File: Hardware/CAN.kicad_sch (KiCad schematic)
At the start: 20 parts, among them U1 ISOW1044

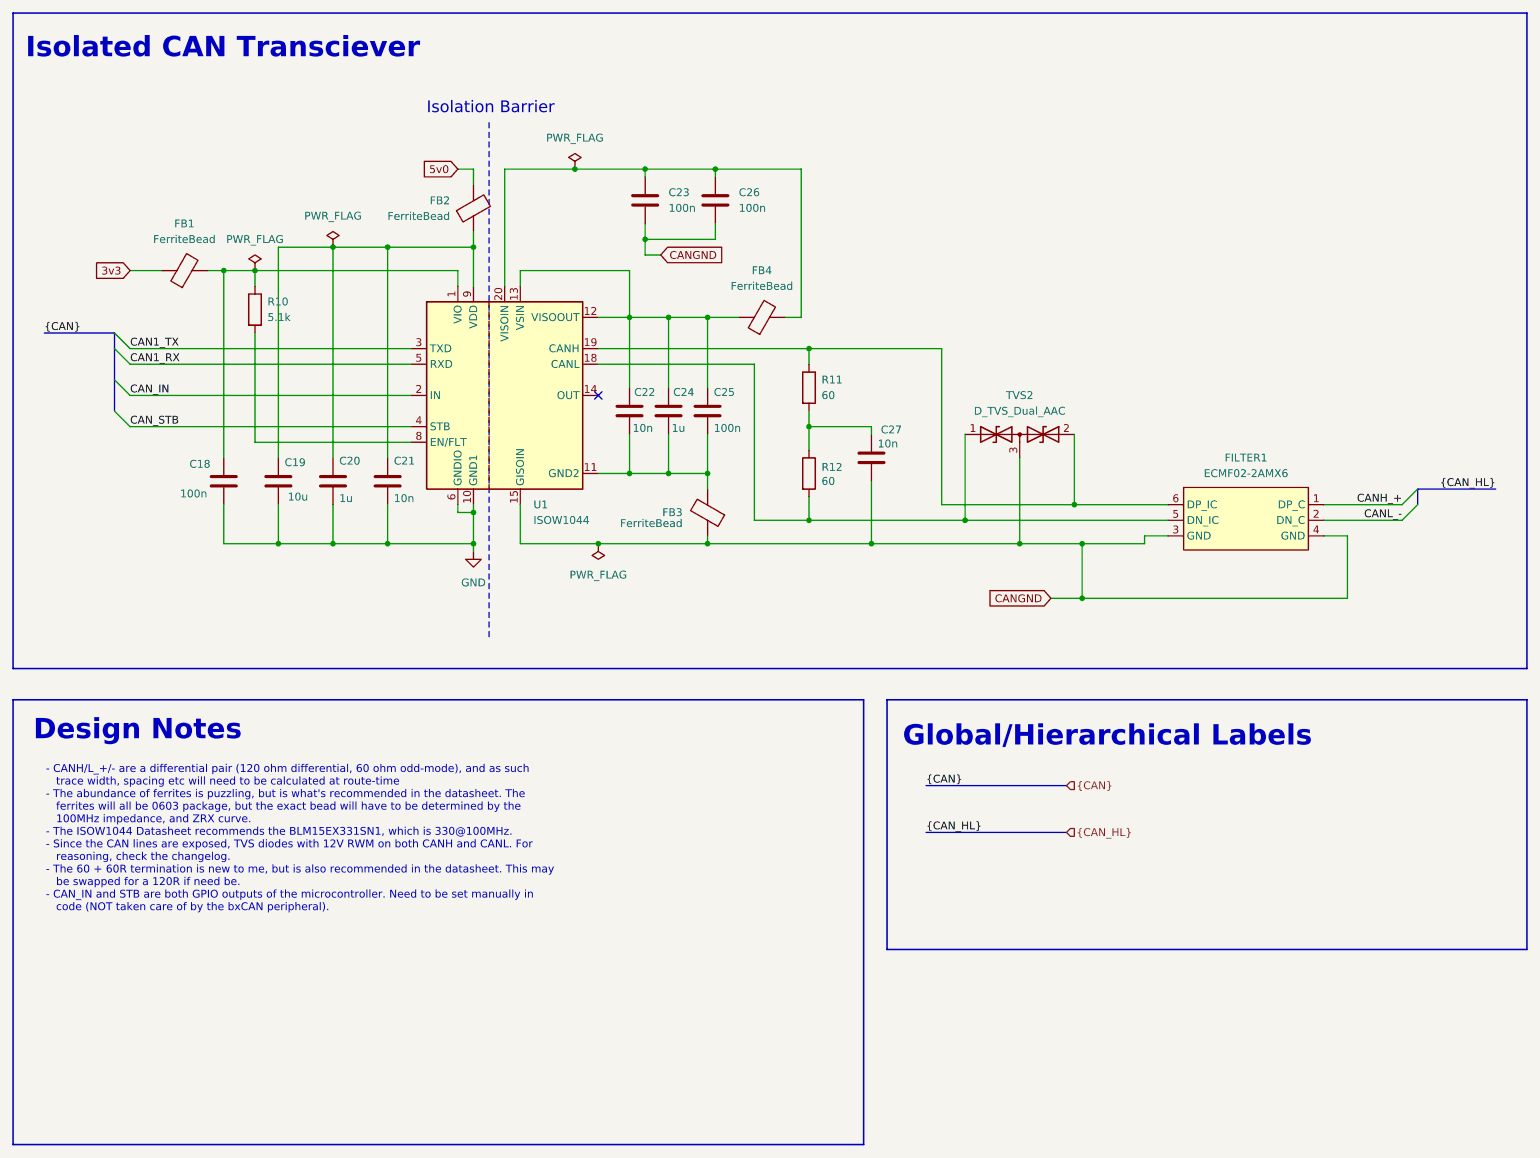
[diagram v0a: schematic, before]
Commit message: Replaced the ISOW1044 CAN Transceiver with the ISO1042 + isolated DC-DC and LDO
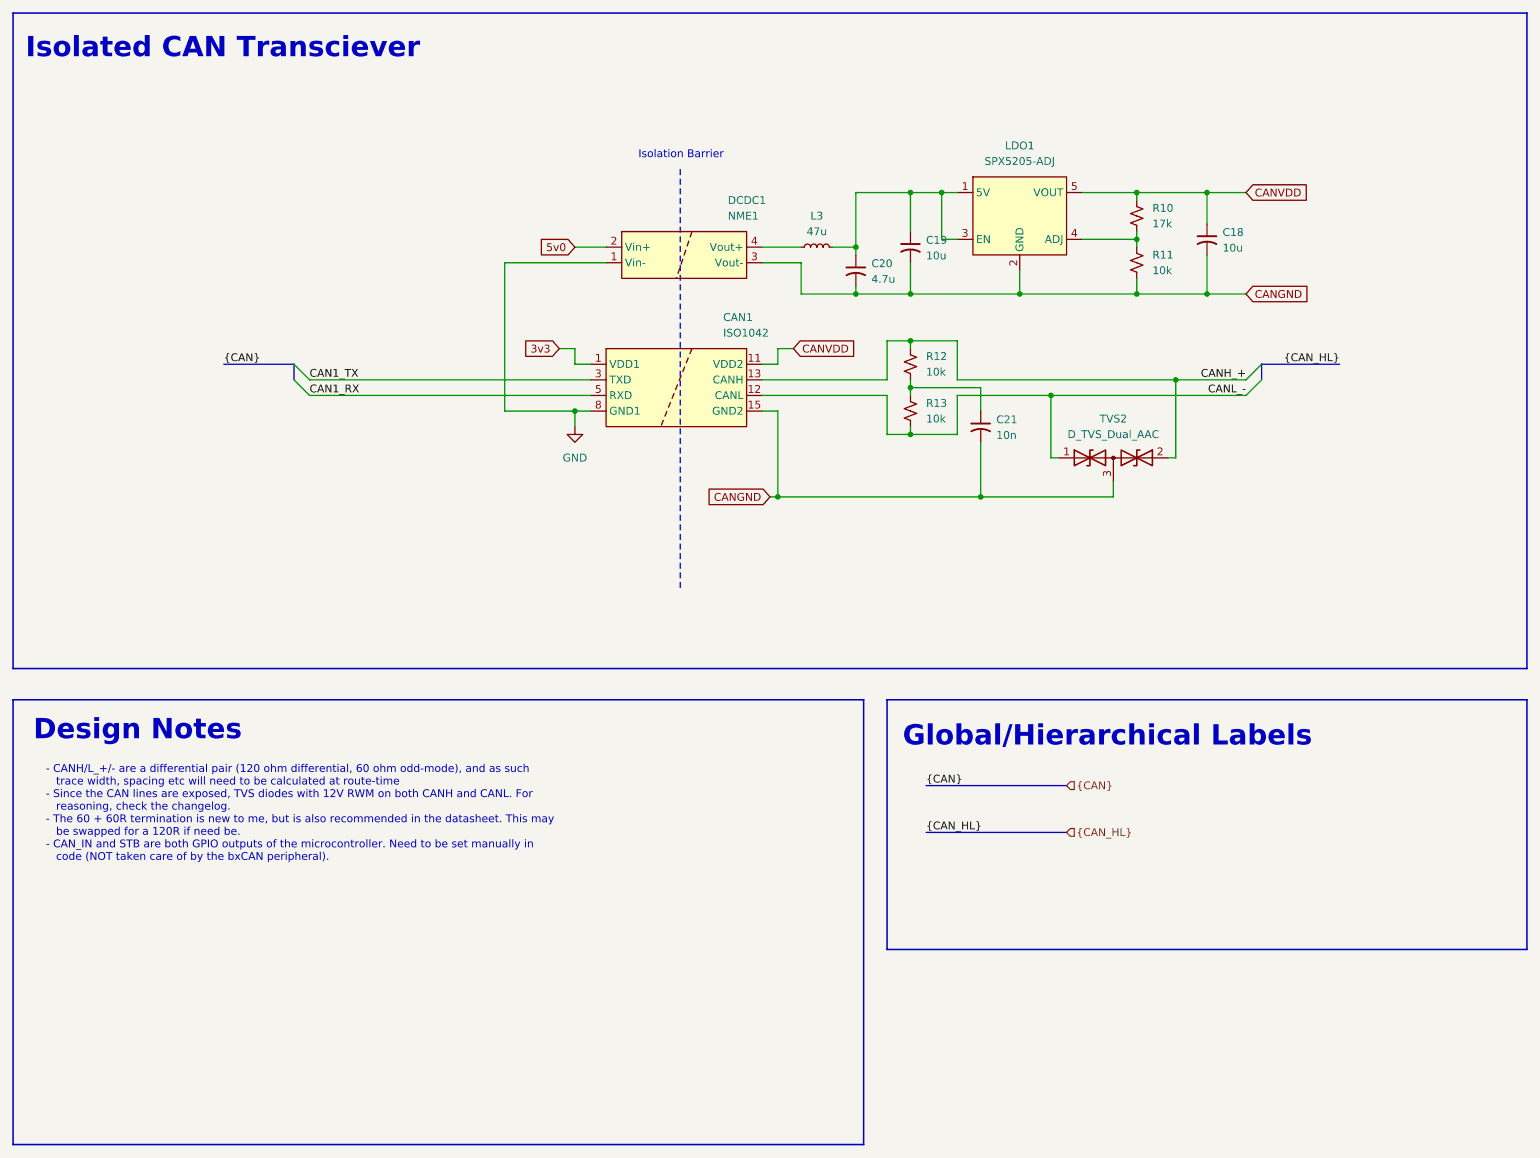
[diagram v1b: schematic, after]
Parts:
- removed C18, C23, C25, C26: 100n, Capacitor_SMD:C_0603_1608Metric_Pad1.08x0.95mm_HandSolder, symbol Device:C
- removed C19: 10u, Capacitor_SMD:C_0603_1608Metric_Pad1.08x0.95mm_HandSolder, symbol Device:C
- removed C20, C24: 1u, Capacitor_SMD:C_0603_1608Metric_Pad1.08x0.95mm_HandSolder, symbol Device:C
- removed C21, C22, C27: 10n, Capacitor_SMD:C_0603_1608Metric_Pad1.08x0.95mm_HandSolder, symbol Device:C
- removed FB1, FB2, FB3, FB4: FerriteBead, Inductor_SMD:L_0603_1608Metric_Pad1.05x0.95mm_HandSolder, symbol Device:FerriteBead
- removed FILTER1: ECMF02-2AMX6, symbol symbols:ECMF2-40A100N6
- removed R10: 5.1k, Resistor_SMD:R_0603_1608Metric_Pad0.98x0.95mm_HandSolder, symbol Device:R
- removed R11, R12: 60, Resistor_SMD:R_0603_1608Metric_Pad0.98x0.95mm_HandSolder, symbol Device:R
- removed U1: ISOW1044, Package_SO:SOIC-20W_7.5x12.8mm_P1.27mm, symbol Interface_CAN_LIN:ISOW1044
- added C18, C19: 10u, symbol Device:C_Small_US
- added C20: 4.7u, symbol Device:C_Small_US
- added C21: 10n, symbol Device:C_Small_US
- added CAN1: ISO1042, symbol symbols:ISO1042
- added DCDC1: NME1, symbol symbols:NME1
- added L3: 47u, symbol Device:L_Small
- added LDO1: SPX5205-ADJ, symbol symbols:SPX5205-ADJ
- added R10: 17k, symbol Device:R_Small_US
- added R11, R12, R13: 10k, symbol Device:R_Small_US
- TVS2: footprint Package_TO_SOT_SMD:SOT-23-3 -> (none)
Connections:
- net 3v3: now also CAN1.1 (VDD1)
- net 5v0: now also DCDC1.2 (Vin+)
- net CAN1_RX: now also CAN1.5 (RXD)
- net CAN1_TX: now also CAN1.3 (TXD)
- net CANH_+: now also TVS2.2 (A2), CAN1.13 (CANH), R12.1
- net CANL_-: now also TVS2.1 (A1), CAN1.12 (CANL), R13.2
- net GND: now also CAN1.2 (GND1), CAN1.8 (GND1), DCDC1.1 (Vin-)
- net CANGND renamed GND2
- net GND2: now also C18.2, C19.2, C20.2, C21.2, CAN1.10 (GND2), CAN1.15 (GND2), CAN1.9 (GND2), DCDC1.3 (Vout-), LDO1.2 (GND), R11.2
- new net: C21.1, R12.2, R13.1
- new net: DCDC1.4 (Vout+), L3.1
- new net: LDO1.4 (ADJ), R10.2, R11.1
- new net: C19.1, C20.1, L3.2, LDO1.1 (5V), LDO1.3 (EN)
- new net: CAN1.4, CAN1.6, CAN1.7
- new net VDD2: C18.1, CAN1.11 (VDD2), CAN1.16 (VDD2), LDO1.5 (VOUT), R10.1
- no-connect marks 1 -> 0
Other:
- note added: "- CANH/L_+/- are a differential pair (120 ohm differential, 60 ohm odd-mode), and as such trace width, spacing etc will need to be calculated at route-time - Since the CAN lines are exposed, TVS diodes with 12V RWM on both CANH and CANL. For reasoning, check the changelog. - The 60 + 60R termination is new to me, but is also recommended in the datasheet. This may be swapped for a 120R if need be.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"
- note removed: "- CANH/L_+/- are a differential pair (120 ohm differential, 60 ohm odd-mode), and as such trace width, spacing etc will need to be calculated at route-time - The abundance of ferrites is puzzling, but is what's recommended in the datasheet. The ferrites will all be 0603 package, but the exact bead will have to be determined by the 100MHz impedance, and ZRX curve. - The ISOW1044 Datasheet recommen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"

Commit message: Updated the USB-C connector from 14 pin to 16 pin
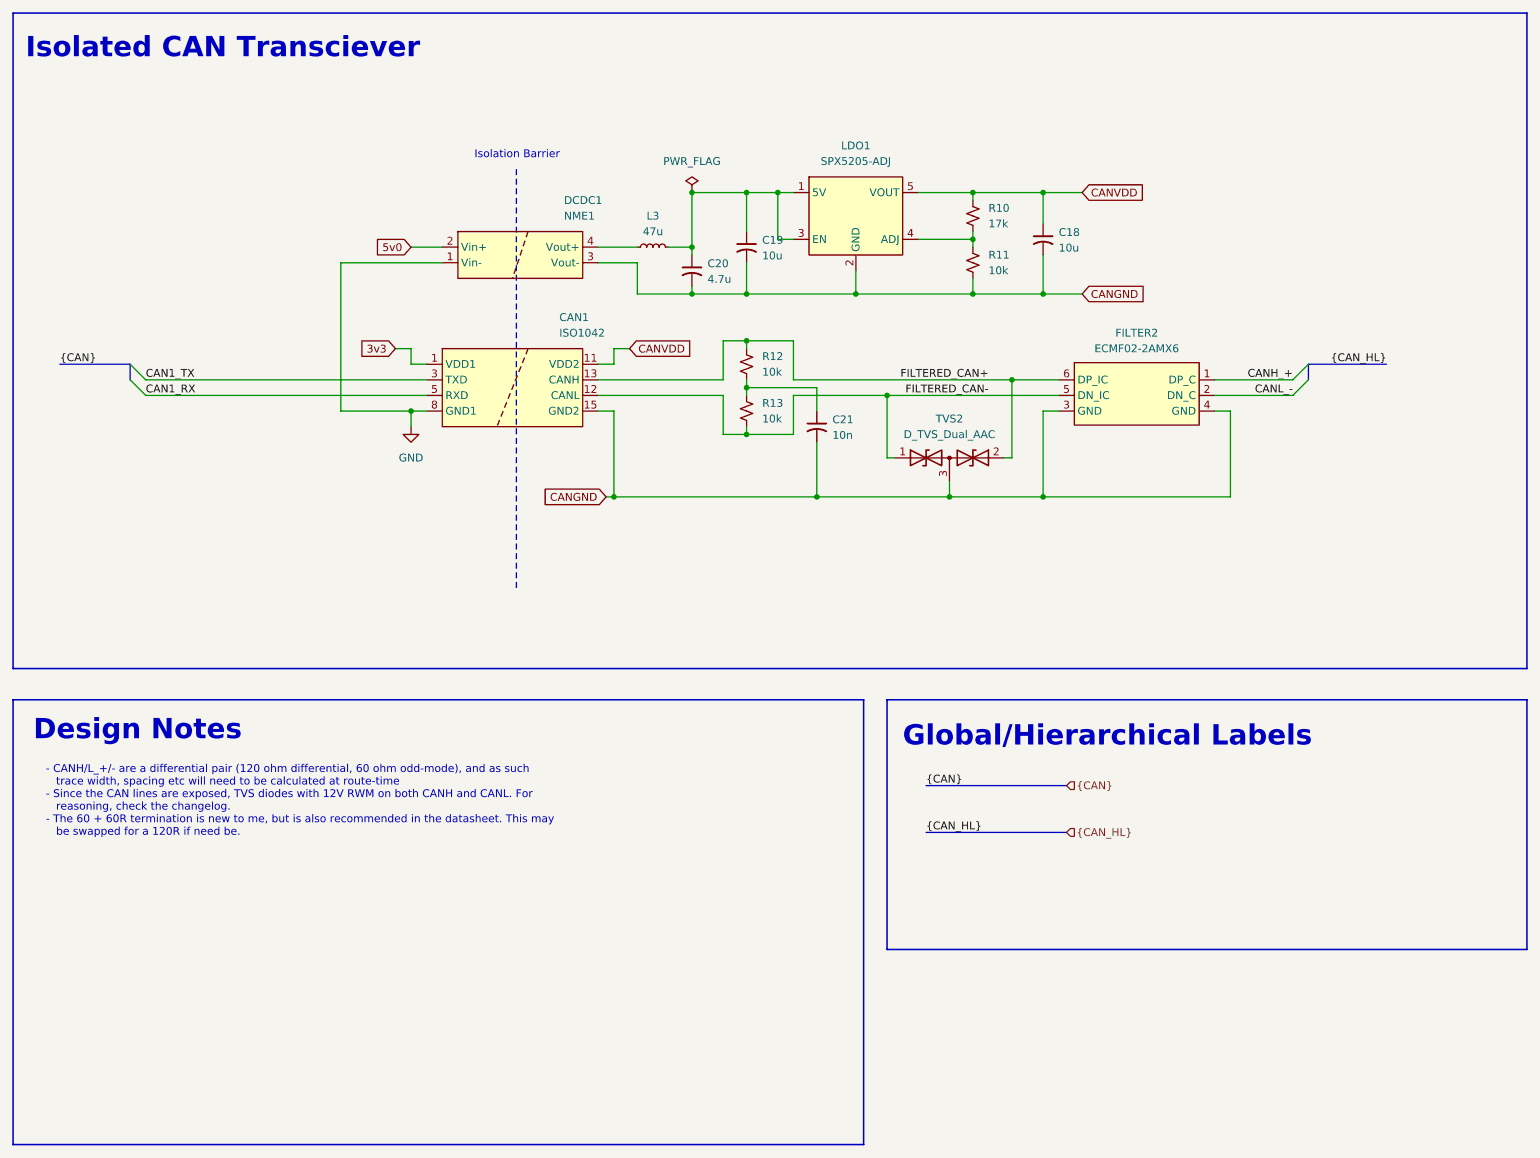
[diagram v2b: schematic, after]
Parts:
- added FILTER2: ECMF02-2AMX6, symbol symbols:ECMF2-40A100N6
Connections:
- net CANH_+: now also FILTER2.1 (DP_C); no longer CAN1.13 (CANH), R12.1, TVS2.2 (A2)
- net CANL_-: now also FILTER2.2 (DN_C); no longer CAN1.12 (CANL), R13.2, TVS2.1 (A1)
- net GND2: now also FILTER2.3 (GND), FILTER2.4 (GND)
- new net FILTERED_CAN+: CAN1.13 (CANH), FILTER2.6 (DP_IC), R12.1, TVS2.2 (A2)
- new net FILTERED_CAN-: CAN1.12 (CANL), FILTER2.5 (DN_IC), R13.2, TVS2.1 (A1)
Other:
- note added: "- CANH/L_+/- are a differential pair (120 ohm differential, 60 ohm odd-mode), and as such trace width, spacing etc will need to be calculated at route-time - Since the CAN lines are exposed, TVS diodes with 12V RWM on both CANH and CANL. For reasoning, check the changelog. - The 60 + 60R termination is new to me, but is also recommended in the datasheet. This may be swapped for a 120R if need be."
- note removed: "- CANH/L_+/- are a differential pair (120 ohm differential, 60 ohm odd-mode), and as such trace width, spacing etc will need to be calculated at route-time - Since the CAN lines are exposed, TVS diodes with 12V RWM on both CANH and CANL. For reasoning, check the changelog. - The 60 + 60R termination is new to me, but is also recommended in the datasheet. This may be swapped for a 120R if need be.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"
- moved on the sheet: C18, C19, C20, C21, CAN1, DCDC1, L3, LDO1, R10, R11, R12, R13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

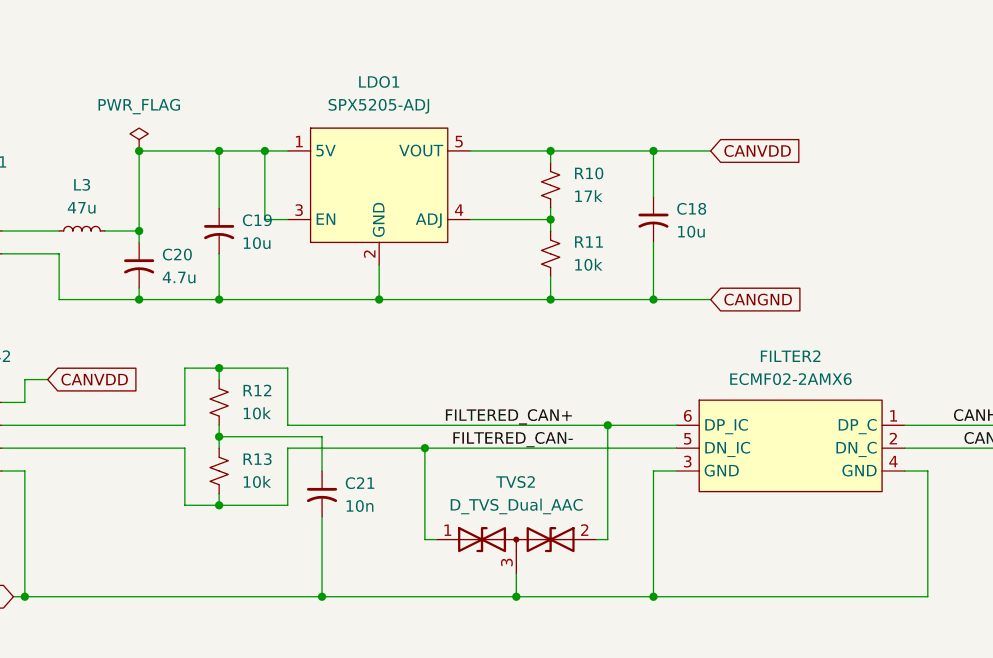
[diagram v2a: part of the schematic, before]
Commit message: Replaced G0B1KET6 with KET6N in schematic
- Updated the schematic with new symbol and pinout.
- Updated the rest of the schematic with all resulting changes
	- This includes the 8 output channels, 7 GPIOs, and slightly
	  different WAGO connector configuration.
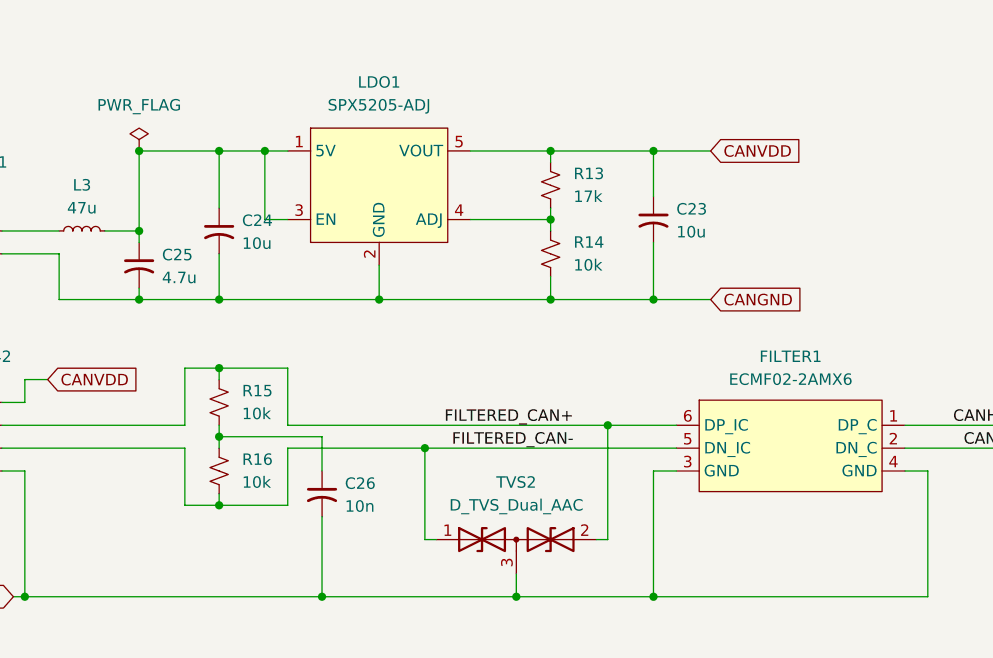
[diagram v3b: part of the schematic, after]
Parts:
- renumbered C18 to C23, C19 to C24, C20 to C25, C21 to C26, FILTER2 to FILTER1, R10 to R13, R11 to R14, R12 to R15, R13 to R16
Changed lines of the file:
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@@
 		(dnp no)
 		(fields_autoplaced yes)
-		(property "Reference" "R13"
+		(property "Reference" "R16"
 			(at 139.7 80.0099 0)
 			(effects
@@
 			(project "CANIO-Board"
 				(path "/a11f98b2-3b09-4cf9-8535-19e509fe91b9/e8300054-67a3-4ec6-9b49-acb4ac45b460"
-					(reference "R13")
+					(reference "R16")
 					(unit 1)
 				)
@@
 		(dnp no)
 		(fields_autoplaced yes)
-		(property "Reference" "R10"
+		(property "Reference" "R13"
 			(at 176.53 48.2599 0)
 			(effects
@@
 			(project ""
 				(path "/a11f98b2-3b09-4cf9-8535-19e509fe91b9/e8300054-67a3-4ec6-9b49-acb4ac45b460"
-					(reference "R10")
+					(reference "R13")
 					(unit 1)
 				)
@@
 		(dnp no)
 		(fields_autoplaced yes)
-		(property "Reference" "#PWR012"
+		(property "Reference" "#PWR013"
 			(at 82.55 90.17 0)
 			(effects
@@
 			(project ""
 				(path "/a11f98b2-3b09-4cf9-8535-19e509fe91b9/e8300054-67a3-4ec6-9b49-acb4ac45b460"
-					(reference "#PWR012")
+					(reference "#PWR013")
 					(unit 1)
 				)
@@
 		(dnp no)
 		(fields_autoplaced yes)
-		(property "Reference" "C20"
+		(property "Reference" "C25"
 			(at 130.81 57.2769 0)
 			(effects
@@
 			(project ""
 				(path "/a11f98b2-3b09-4cf9-8535-19e509fe91b9/e8300054-67a3-4ec6-9b49-acb4ac45b460"
-					(reference "C20")
+					(reference "C25")
 					(unit 1)
 				)
@@
 		(dnp no)
 		(fields_autoplaced yes)
-		(property "Reference" "R12"
+		(property "Reference" "R15"
 			(at 139.7 72.3899 0)
 			(effects
@@
 			(project "CANIO-Board"
 				(path "/a11f98b2-3b09-4cf9-8535-19e509fe91b9/e8300054-67a3-4ec6-9b49-acb4ac45b460"
-					(reference "R12")
+					(reference "R15")
 					(unit 1)
 				)
@@
 		(dnp no)
 		(fields_autoplaced yes)
-		(property "Reference" "R11"
+		(property "Reference" "R14"
 			(at 176.53 55.8799 0)
 			(effects
@@
 			(project "CANIO-Board"
 				(path "/a11f98b2-3b09-4cf9-8535-19e509fe91b9/e8300054-67a3-4ec6-9b49-acb4ac45b460"
-					(reference "R11")
+					(reference "R14")
 					(unit 1)
 				)
@@
 		(dnp no)
 		(fields_autoplaced yes)
-		(property "Reference" "FILTER2"
+		(property "Reference" "FILTER1"
 			(at 200.66 68.58 0)
 			(effects
@@
 			(project "CANIO-Board"
 				(path "/a11f98b2-3b09-4cf9-8535-19e509fe91b9/e8300054-67a3-4ec6-9b49-acb4ac45b460"
-					(reference "FILTER2")
+					(reference "FILTER1")
 					(unit 1)
 				)
@@
 		(dnp no)
 		(fields_autoplaced yes)
-		(property "Reference" "C18"
+		(property "Reference" "C23"
 			(at 187.96 52.1969 0)
 			(effects
@@
 			(project "CANIO-Board"
 				(path "/a11f98b2-3b09-4cf9-8535-19e509fe91b9/e8300054-67a3-4ec6-9b49-acb4ac45b460"
-					(reference "C18")
+					(reference "C23")
 					(unit 1)
 				)
@@
 		(dnp no)
 		(fields_autoplaced yes)
-		(property "Reference" "C21"
+		(property "Reference" "C26"
 			(at 151.13 82.6769 0)
 			(effects
@@
 			(project "CANIO-Board"
 				(path "/a11f98b2-3b09-4cf9-8535-19e509fe91b9/e8300054-67a3-4ec6-9b49-acb4ac45b460"
-					(reference "C21")
+					(reference "C26")
 					(unit 1)
 				)
@@
 		(dnp no)
 		(fields_autoplaced yes)
-		(property "Reference" "C19"
+		(property "Reference" "C24"
 			(at 139.7 53.4669 0)
 			(effects
@@
 			(project "CANIO-Board"
 				(path "/a11f98b2-3b09-4cf9-8535-19e509fe91b9/e8300054-67a3-4ec6-9b49-acb4ac45b460"
-					(reference "C19")
-					(unit 1)
-				)
+					(reference "C24")
+					(unit 1)
+				)
